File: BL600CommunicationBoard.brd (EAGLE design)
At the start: 65.7 x 67.3 mm, 26 parts, among them IC1 MAX3218, IC2 LM2937ET, IC3 MAX3218, X1 RS-232

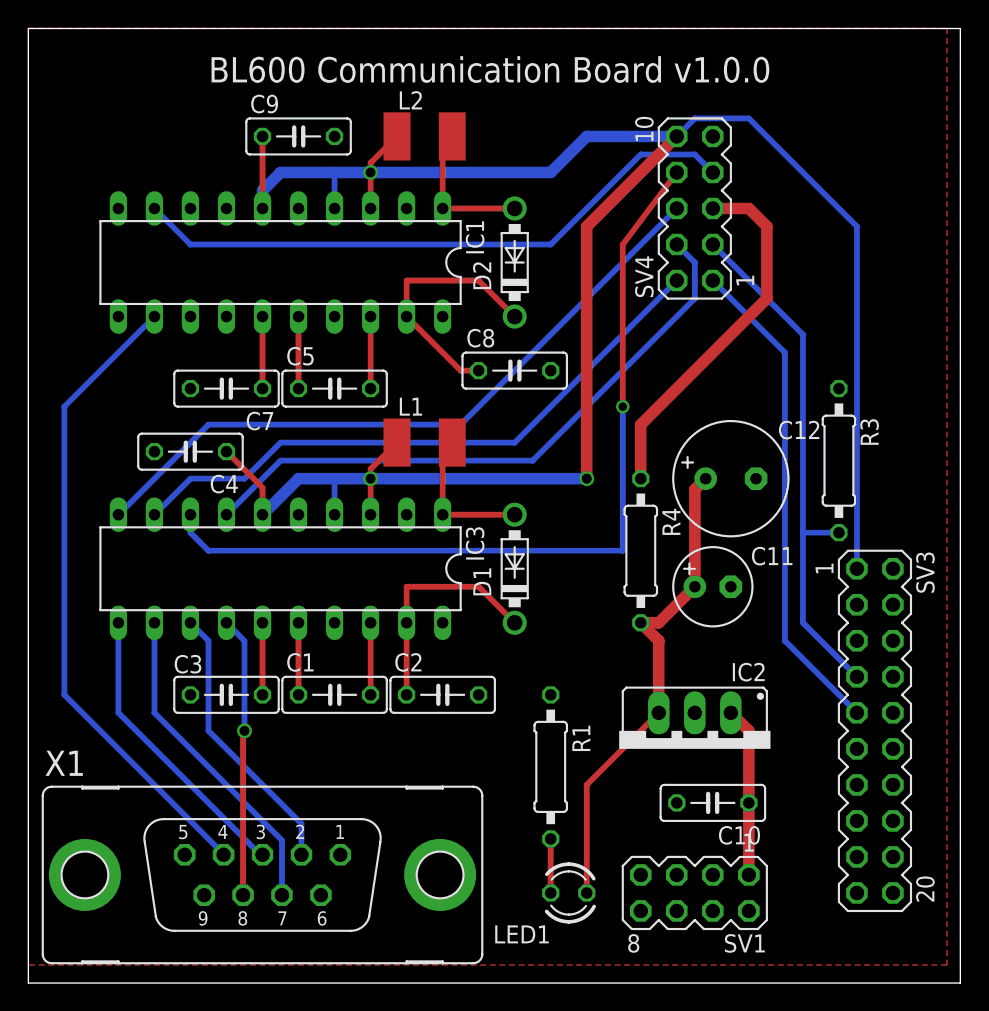
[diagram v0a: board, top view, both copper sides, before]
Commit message: Change placement of header pin for communication board, and changed to vector text in windVane layout
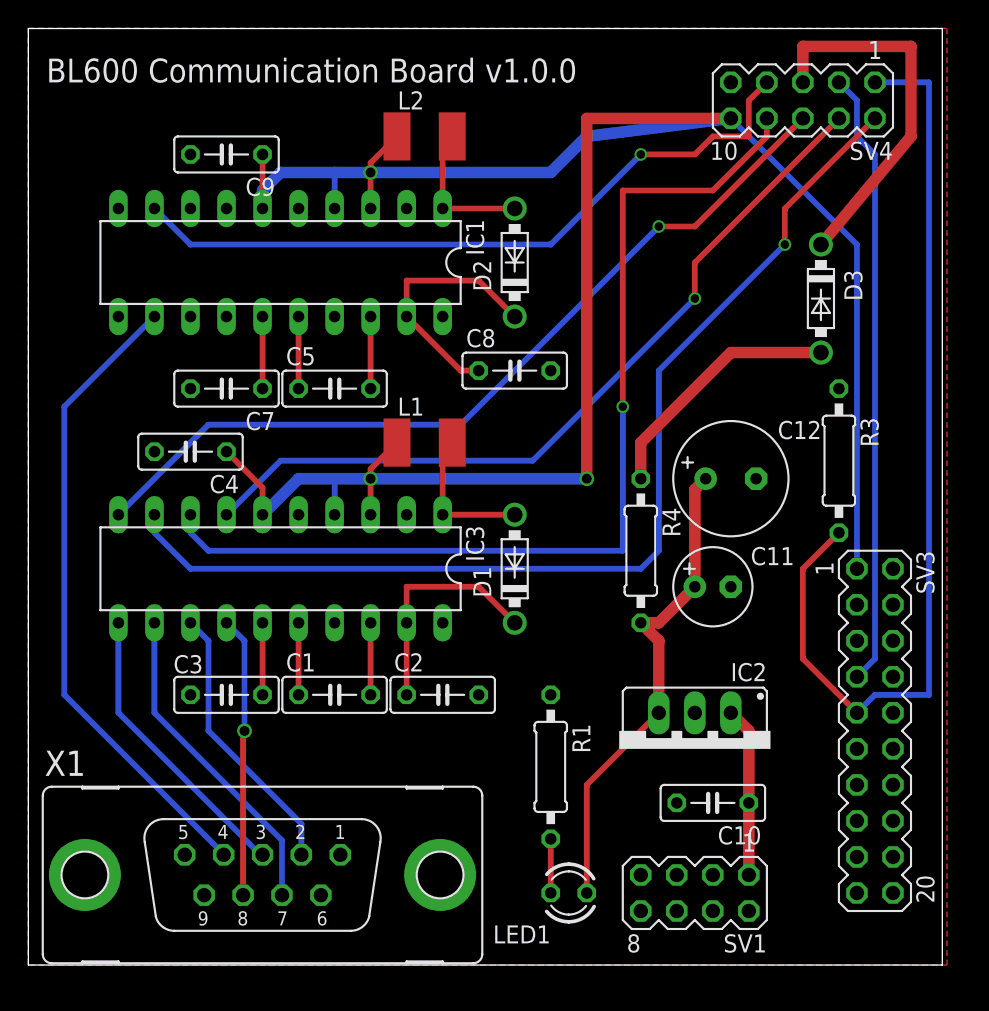
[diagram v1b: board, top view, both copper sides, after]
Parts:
- added D3: 1N5817-T, diode:DO41-7.6
- moved SV4 10.8 mm to (59.7, 61.0), turned to 180 degrees
- moved C9 5.24 mm to (19.1, 57.1), turned to 180 degrees
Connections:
- removed net N$17: R4.1, SV4.5
- new net N$6: D3.A, R4.1
- new net N$7: D3.C, SV4.5
- net NRESET/SWDIO/TMS: no longer R3.2
- net SWDCLK/TCK: now also R3.2
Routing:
- net SWDCLK/TCK: track 34.7 -> 67.9 mm
- net N$4: track 43.7 -> 75.2 mm, vias 0 -> 1
- net N$7: track 0.00 -> 26.4 mm
- net N$17: track 25.8 -> 0.00 mm
- net N$6: track 0.00 -> 17.9 mm
- net N$3: track 43.7 -> 56.2 mm, vias 0 -> 1
- net N$5: track 48.3 -> 59.8 mm, vias 0 -> 1
- net N$2: track 60.2 -> 70.7 mm
- net 1V8: track 150.6 -> 159.5 mm
- net N$24: track 43.6 -> 50.5 mm, vias 0 -> 1
- net NRESET/SWDIO/TMS: track 37.2 -> 43.5 mm
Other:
- board size 65.7 x 67.3 mm -> 64.4 x 66 mm
